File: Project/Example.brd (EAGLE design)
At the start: 86 x 54 mm, 14 parts, among them IC1 LM555D, J2 UX60-MB-5S8, Q1 BSS806N, Q2 SSM3J356R, SW1 MFS101D-6-Z

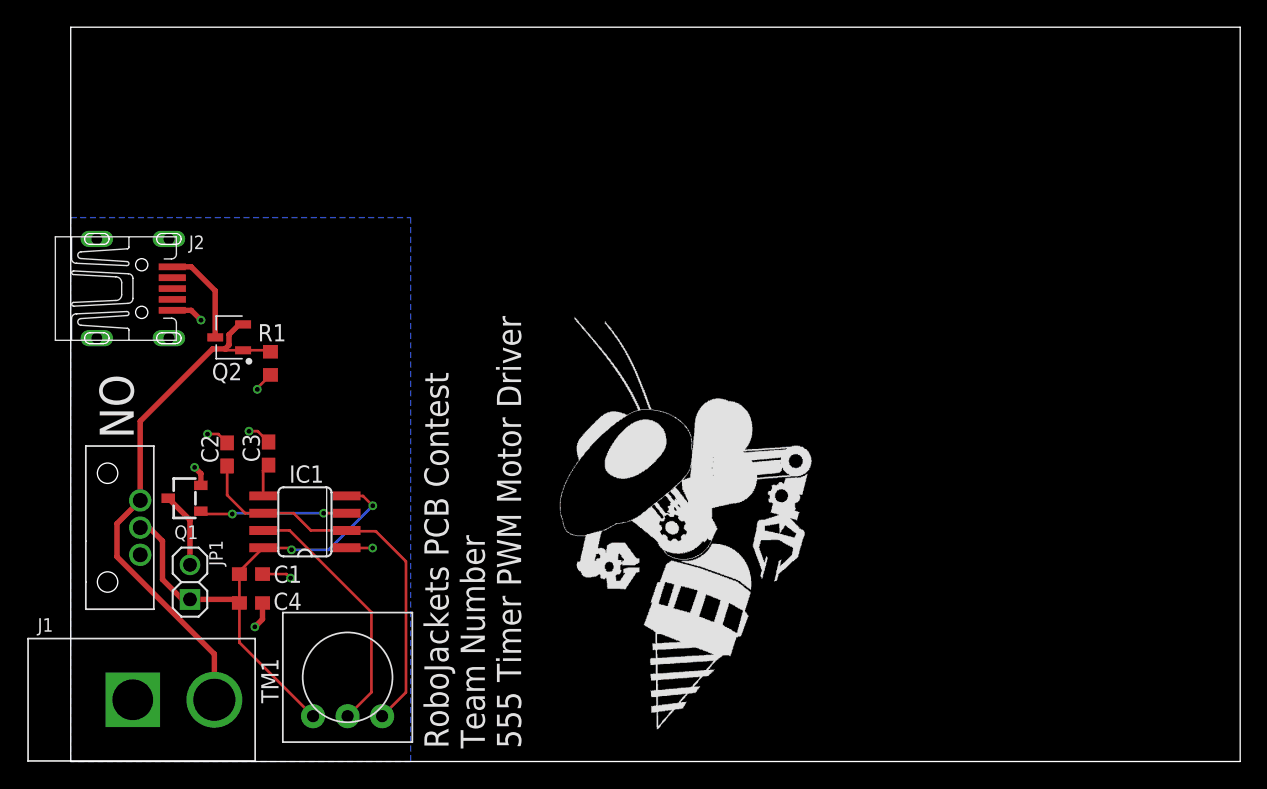
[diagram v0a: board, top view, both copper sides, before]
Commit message: Made schematic neater
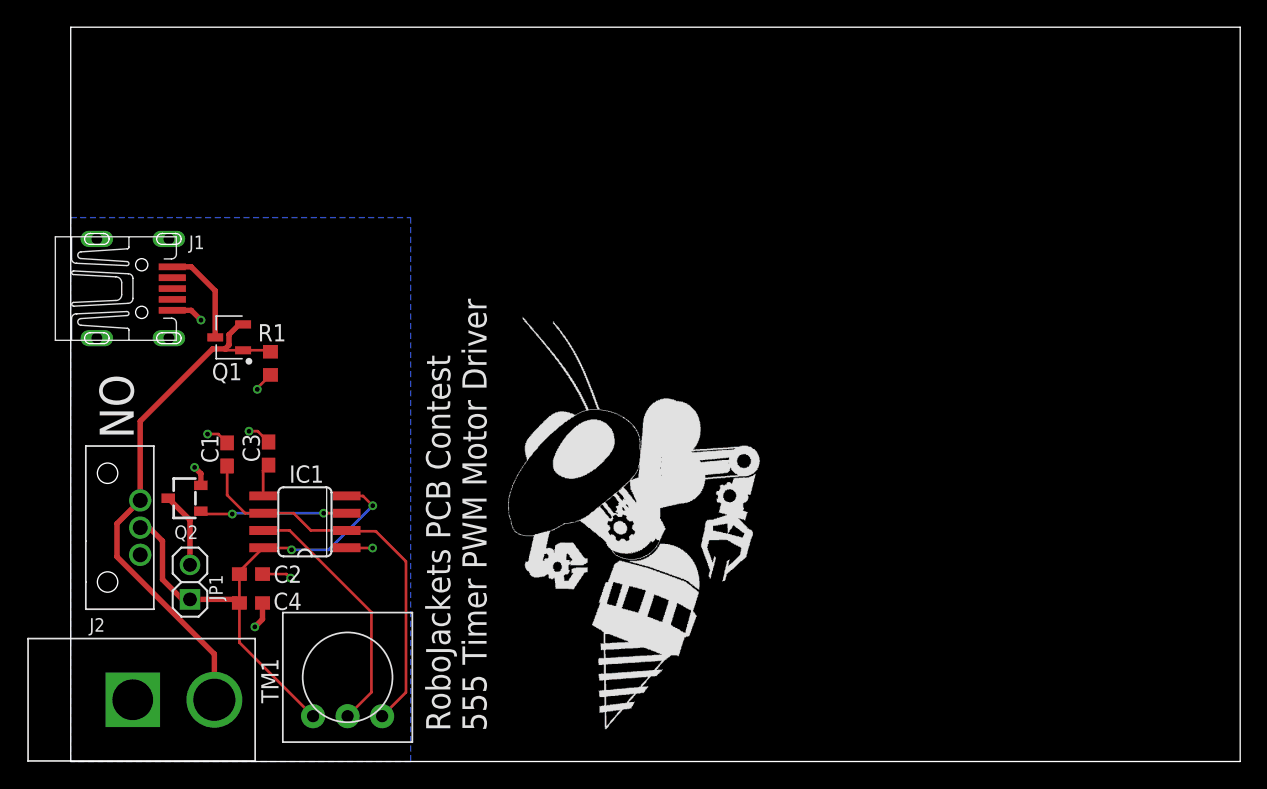
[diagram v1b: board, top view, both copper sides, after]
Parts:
- C1: value .1uF -> 0.01uF
- C2: value .01uF -> .1uF
- C3: value .01uF -> 0.01uF
- J1: value (none) -> UX60-MB-5S8; device RoboJackets-Connectors:PJ-037A -> RoboJackets-Connectors:UX60-MB-5S8
- J2: value UX60-MB-5S8 -> (none); device RoboJackets-Connectors:UX60-MB-5S8 -> RoboJackets-Connectors:PJ-037A
- Q1: value BSS806N -> SSM3J356R; device RoboJackets-Discrete:SOT-23-3 -> Example:SOT95P240X80-3N
- Q2: value SSM3J356R -> BSS806N; device Example:SOT95P240X80-3N -> RoboJackets-Discrete:SOT-23-3
- moved J1 30.8 mm to (-1.18, 34.8)
- moved J2 30.8 mm to (4.56, 4.54)
- moved Q1 12.3 mm to (11.7, 31.2), turned to 180 degrees
- moved Q2 12.3 mm to (8.37, 19.4), turned to 90 degrees
- moved C1 8.97 mm to (11.5, 22.6), turned to 90 degrees
- moved C2 8.97 mm to (13.3, 13.8), turned to 0 degrees
- moved U$2 3.81 mm to (39.2, 2.36)
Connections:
- net +9V: now also C2.1; no longer C1.1
- net GND: now also J1.5, J2.P$1, Q2.2; no longer J1.P$1, J2.5, Q1.2
- net N$2: now also Q2.3; no longer Q1.3
- net N$4: now also J1.1, Q1.3; no longer J2.1, Q2.3
- net N$6: now also J2.P$2, Q1.1, Q1.2; no longer J1.P$2, Q2.1, Q2.2
- net THR: now also C1.1; no longer C2.1
- net T_OUT: now also Q2.1; no longer Q1.1
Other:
- board text added: "RoboJackets PCB Contest 555 Timer PWM Motor Driver"
- board text removed: "RoboJackets PCB Contest Team Number 555 Timer PWM Motor Driver"
